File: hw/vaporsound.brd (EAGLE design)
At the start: 100 x 80 mm, 80 parts, among them Q1 BSS138, Q2 BSS138, X1 MSTBV2, X2 MSTBV2, X3 MSTBV2

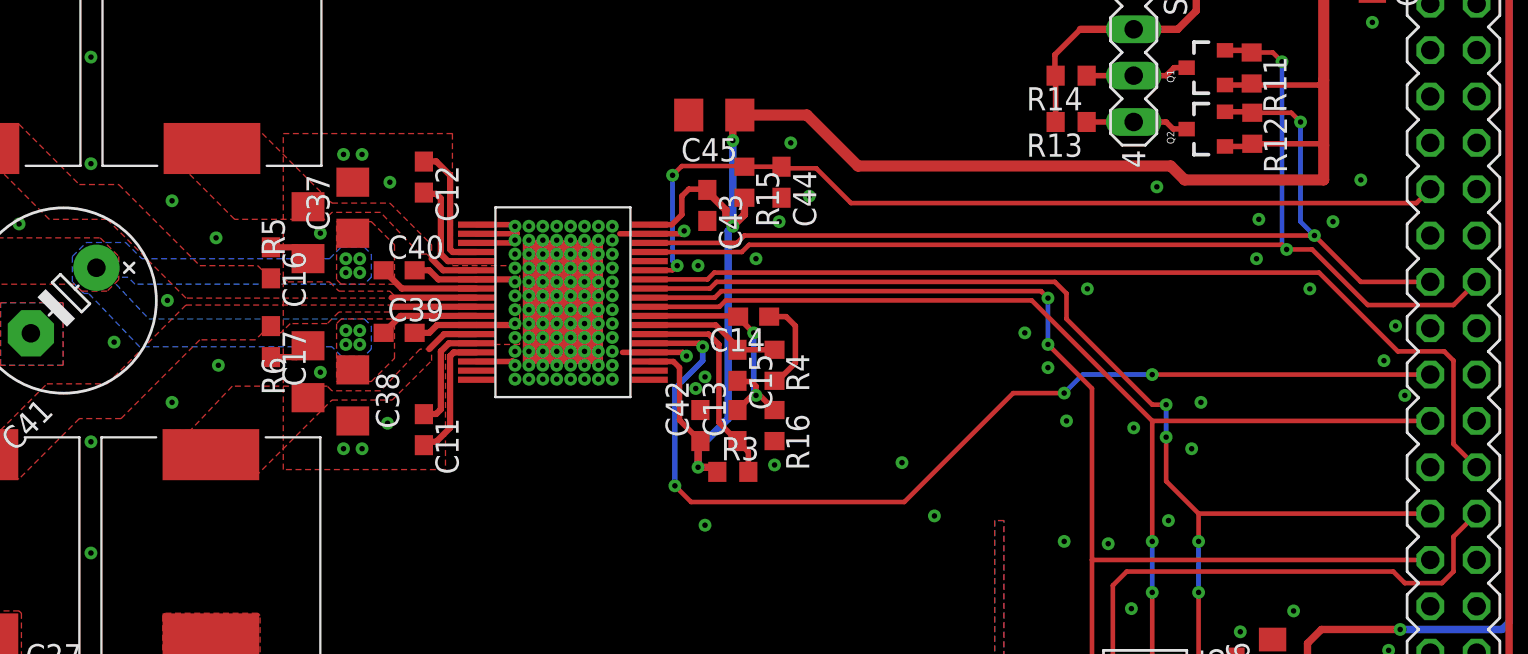
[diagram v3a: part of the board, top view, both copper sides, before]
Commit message: Add pullup and pulldown STA350BW + minor layout fixes
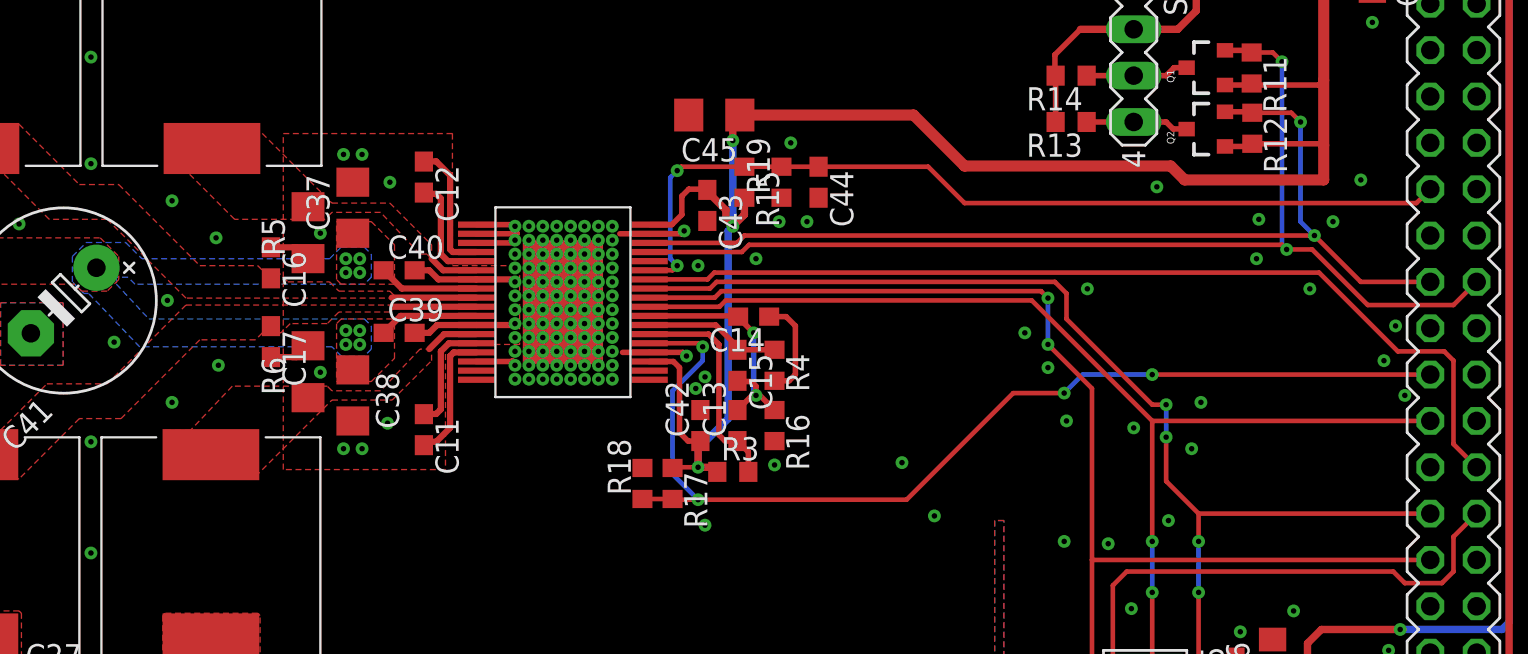
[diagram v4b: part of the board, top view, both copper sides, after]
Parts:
- added R17, R18, R19: DNP, rcl:R0603
- moved C44 2.03 mm to (60.5, 47.4)
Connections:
- net +3V3: now also R17.1
- net GND: now also R18.2, R19.1
- net POWERDOWN: now also R17.2, R18.1
- net RESET: now also R19.2
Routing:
- net POWERDOWN: track 55.9 -> 59.4 mm
- net +3V3: track 164.7 -> 166.3 mm
- net N$11: track 5.23 -> 5.76 mm

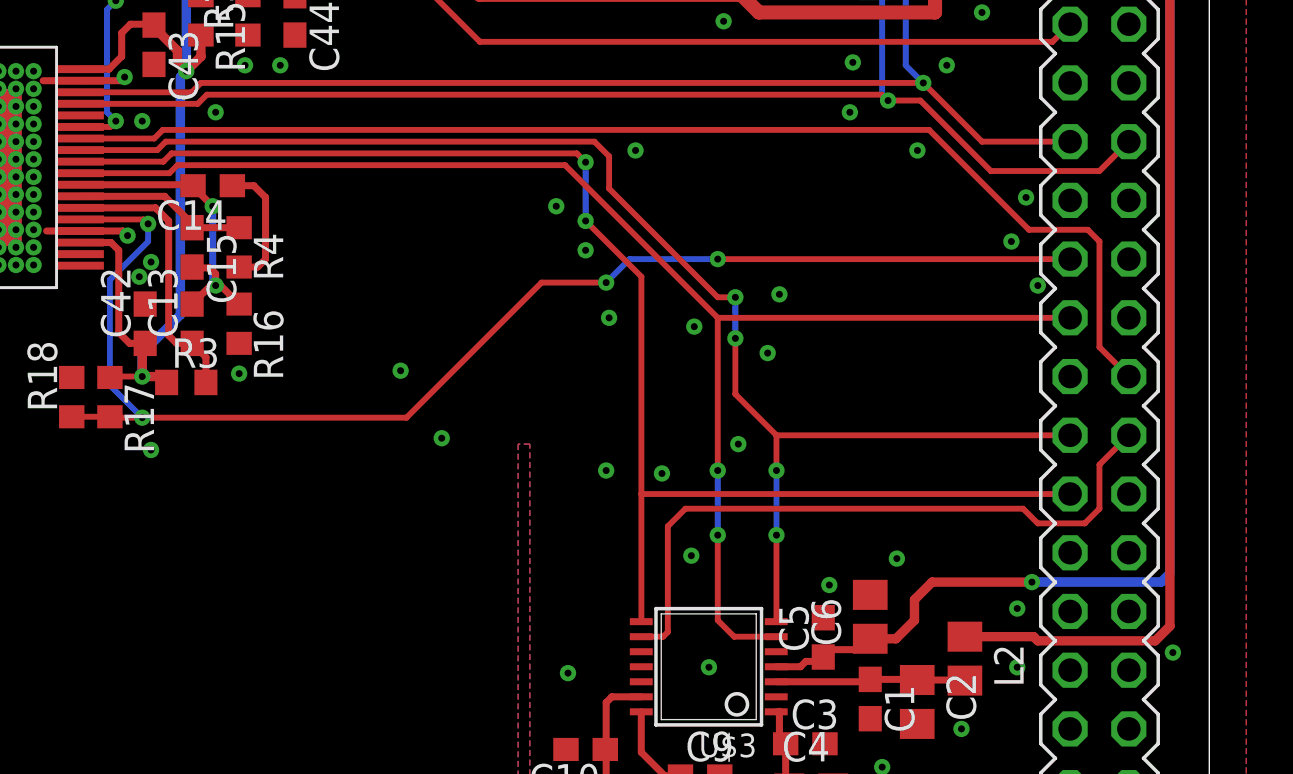
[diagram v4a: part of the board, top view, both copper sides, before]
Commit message: Reroute I2S connections
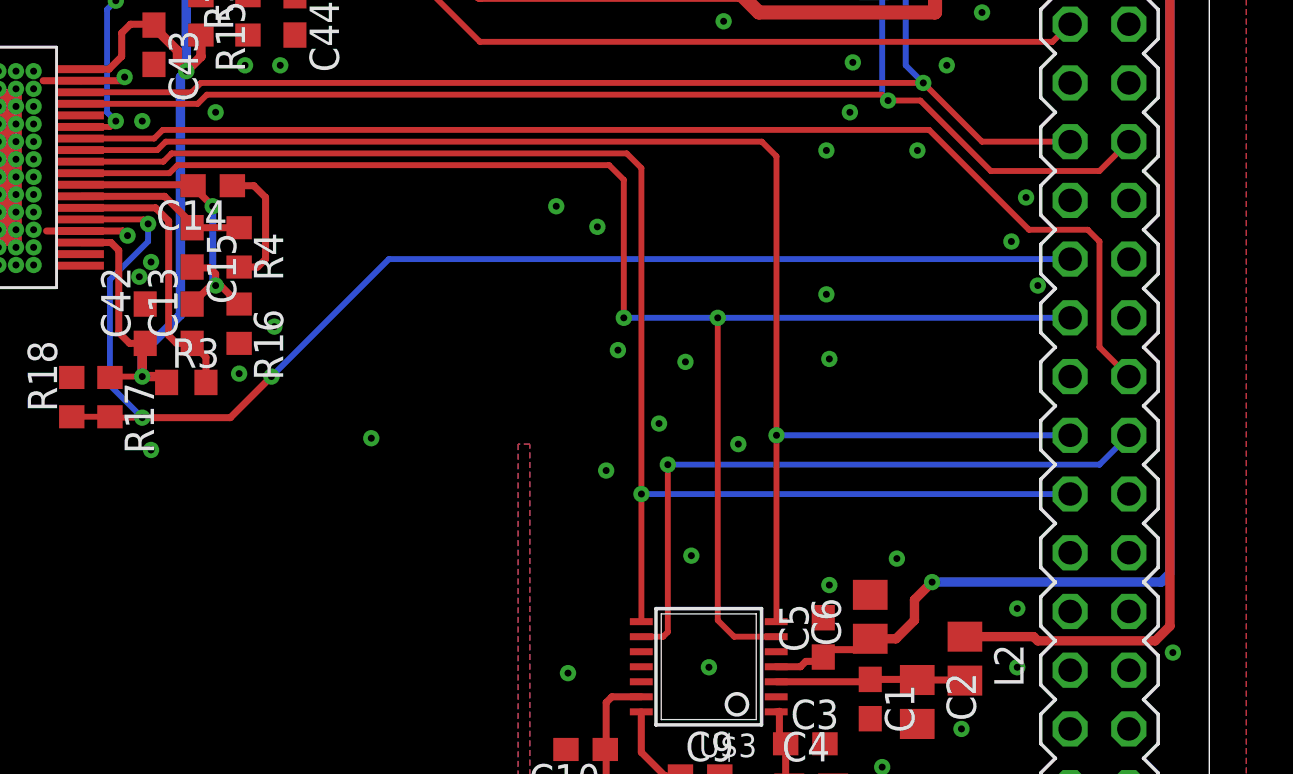
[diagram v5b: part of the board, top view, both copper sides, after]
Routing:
- net LRCK: track 59.5 -> 63.3 mm, vias 4 -> 1
- net MCK: track 61.6 -> 65.1 mm
- net BCK: track 61.6 -> 62.8 mm, vias 2 -> 1
- net D_ADC: track 29.0 -> 28.9 mm, vias 0 -> 1
- net POWERDOWN: vias 4 -> 3

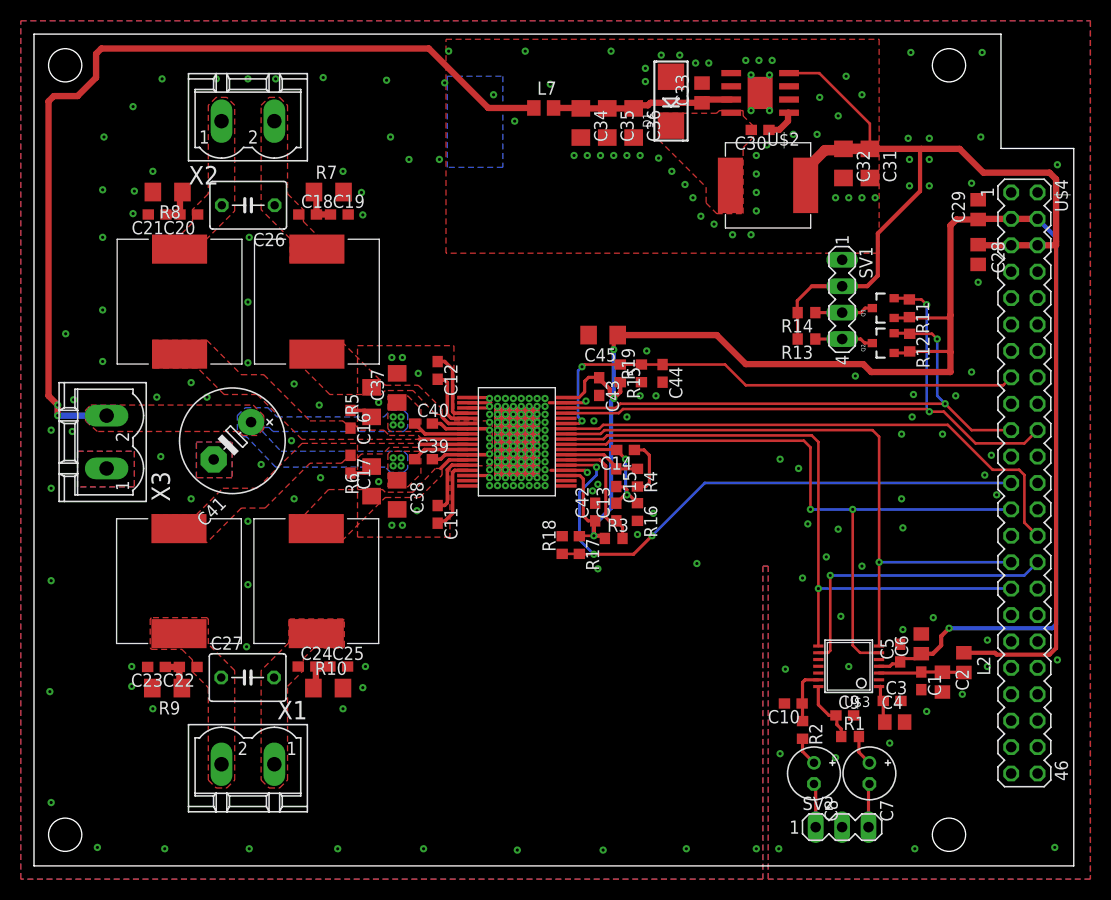
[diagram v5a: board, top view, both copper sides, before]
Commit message: ground plane stitching + thermal vias
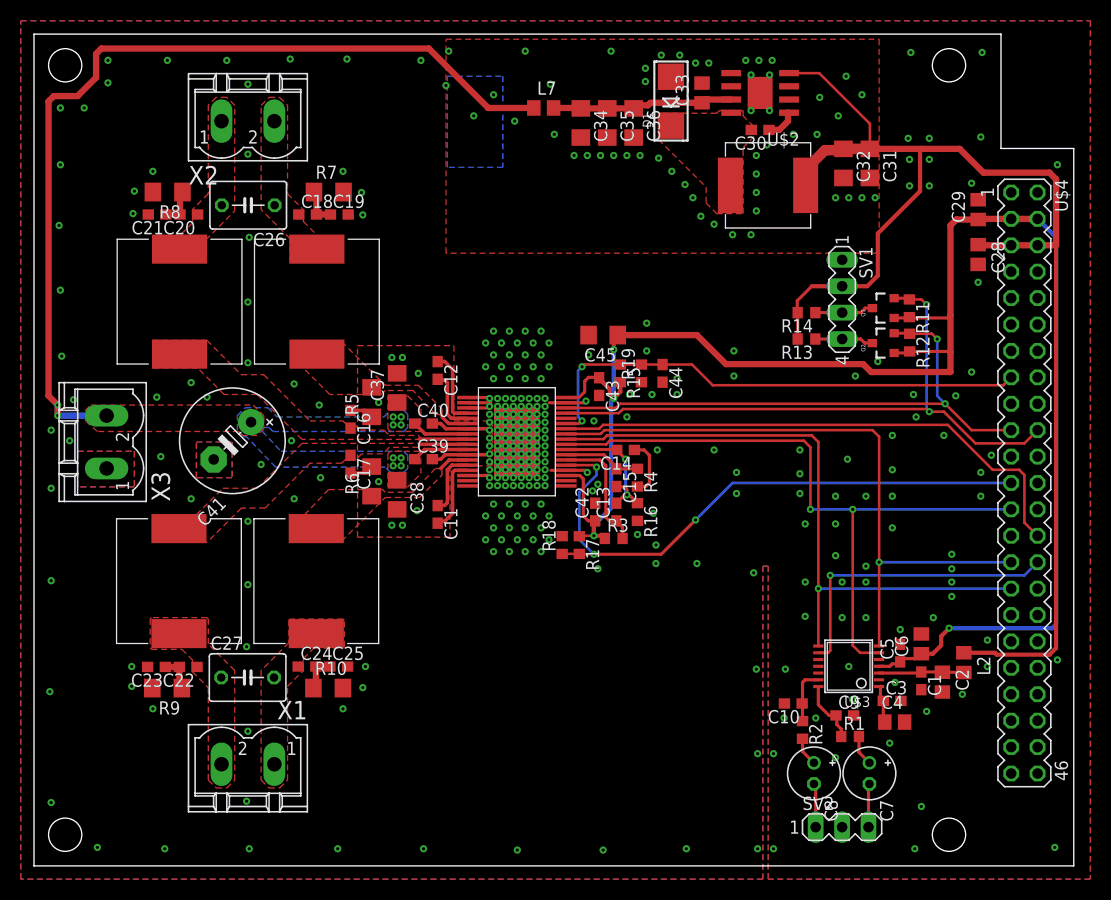
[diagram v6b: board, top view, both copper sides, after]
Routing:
- net GND: vias 274 -> 355

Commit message: silkscreen
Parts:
- moved C29 0.38 mm to (90.4, 63.1)
- renumbered SV1 to DISP, SV2 to IN, U$4 to P9, X1 to SPKR1, X2 to SPKR2, X3 to PWR
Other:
- board text added: "+24V"
- board text added: "GND"
- board text added: "Rev. 0.1"
- board text added: "entropia.de/vaporsound"
